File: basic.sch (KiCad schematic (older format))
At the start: 9 parts, among them J5 Conn_02x02_Top_Bottom, X1 dummy, X2 dummy

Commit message: Power Sch. Updated.
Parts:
- gave numbers to parts that had none: 4
- renumbered FID2 to FID3, J5 to J1
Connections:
- net GND renamed VIN_GND
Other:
- note removed: "TODO\n- breakout modem signals\n- TI DCDC might need to be set to 3.4V, \ncheck datasheets of all the stuff\n- MCP73223 UVLO is too low?\n- OPAMP for sense"
- moved on the sheet: J1
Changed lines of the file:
@@
 $EndComp
 Wire Wire Line
-	2850 3500 2650 3500
-$Comp
-L Mechanical:Fiducial FID2
+	3200 3550 3000 3550
+$Comp
+L Mechanical:Fiducial FID3
 U 1 1 5E789C24
 P 7700 5900
-F 0 "FID2" H 7785 5946 50  0000 L CNN
+F 0 "FID3" H 7785 5946 50  0000 L CNN
 F 1 "Fiducial" H 7785 5855 50  0000 L CNN
 F 2 "Aesthetics:FIDUCIAL-1X2" H 7700 5900 50  0001 C CNN
@@
 	1    0    0    -1
 $EndComp
-Text GLabel 2850 3500 2    50   Input ~ 0
+Text GLabel 3200 3550 2    50   Input ~ 0
 VIN_12V
 $Comp
-L Connector_Generic:Conn_02x02_Top_Bottom J5
+L Connector_Generic:Conn_02x02_Top_Bottom J1
 U 1 1 5E789BF0
-P 2350 3500
-F 0 "J5" H 2400 3250 50  0000 C CNN
-F 1 "Conn_02x02_Top_Bottom" H 2400 3700 50  0000 C CNN
-F 2 "Connector_Molex:Molex_Micro-Fit_3.0_43045-0400_2x02_P3.00mm_Horizontal" H 2350 3500 50  0001 C CNN
-F 3 "~" H 2350 3500 50  0001 C CNN
-	1    2350 3500
-	1    0    0    -1
-$EndComp
-Text Notes 950  6550 0    64   ~ 0
-TODO\n- breakout modem signals\n- TI  DCDC might need to be set to 3.4V, \ncheck datasheets of all the stuff\n- MCP73223 UVLO is too low?\n- OPAMP for sense
+P 2700 3550
+F 0 "J1" H 2750 3300 50  0000 C CNN
+F 1 "Conn_02x02_Top_Bottom" H 2750 3750 50  0000 C CNN
+F 2 "Connector_Molex:Molex_Micro-Fit_3.0_43045-0400_2x02_P3.00mm_Horizontal" H 2700 3550 50  0001 C CNN
+F 3 "~" H 2700 3550 50  0001 C CNN
+	1    2700 3550
+	1    0    0    -1
+$EndComp
 $Sheet
 S 4000 2400 1000 1000
@@
 F0 "power" 50
 F1 "power.sch" 50
+F2 "CHARGE_STAT" O R 5000 3100 50
+F3 "CHARGER_EN" I R 5000 3200 50
 $EndSheet
 $Comp
@@
 Wire Wire Line
 	5500 4400 5000 4400
-Text GLabel 2850 3600 2    50   Input ~ 0
+Text GLabel 3200 3650 2    50   Input ~ 0
 CANH
-Text GLabel 1900 3600 0    50   Input ~ 0
+Text GLabel 2250 3650 0    50   Input ~ 0
 CANL
 Wire Wire Line
-	2850 3600 2650 3600
+	3200 3650 3000 3650
 $Sheet
 S 5500 3000 1500 1500
@@
 F2 "TWIO_SCK" B R 7000 3100 50
 F3 "TWIO_SDA" B R 7000 3200 50
-F4 "CHARGE_STAT" I L 5500 3100 50
-F5 "CAN0IRQ" I L 5500 4400 50
-F6 "MISO" I L 5500 4000 50
-F7 "MOSI" O L 5500 4100 50
-F8 "SCLK" O L 5500 4200 50
-F9 "CSO" O L 5500 4300 50
-F10 "MODEM_TX" I R 7000 4300 50
-F11 "MODEM_RX" O R 7000 4400 50
-F12 "MODEM_RELAIS" O R 7000 4100 50
-F13 "MODEM_DTR" O R 7000 3900 50
-F14 "MODEM_WDISABLE" O R 7000 4200 50
-F15 "MODEM_RESET" O R 7000 4000 50
-F16 "IMU_INT1" I R 7000 3300 50
-$EndSheet
-$Comp
-L Mechanical:Fiducial FID?
+F4 "CAN0IRQ" I L 5500 4400 50
+F5 "MISO" I L 5500 4000 50
+F6 "MOSI" O L 5500 4100 50
+F7 "SCLK" O L 5500 4200 50
+F8 "CSO" O L 5500 4300 50
+F9 "MODEM_TX" I R 7000 4300 50
+F10 "MODEM_RX" O R 7000 4400 50
+F11 "MODEM_RELAIS" O R 7000 4100 50
+F12 "MODEM_DTR" O R 7000 3900 50
+F13 "MODEM_WDISABLE" O R 7000 4200 50
+F14 "MODEM_RESET" O R 7000 4000 50
+F15 "IMU_INT1" I R 7000 3300 50
+F16 "CHARGE_STAT" I L 5500 3100 50
+F17 "CHARGER_EN" O L 5500 3200 50
+$EndSheet
+$Comp
+L Mechanical:Fiducial FID5
 U 1 1 605974C2
 P 8200 5900
-F 0 "FID?" H 8285 5946 50  0000 L CNN
+F 0 "FID5" H 8285 5946 50  0000 L CNN
 F 1 "Fiducial" H 8285 5855 50  0000 L CNN
 F 2 "Aesthetics:FIDUCIAL-1X2" H 8200 5900 50  0001 C CNN
@@
 $EndComp
 $Comp
-L Mechanical:Fiducial FID?
+L Mechanical:Fiducial FID2
 U 1 1 60597847
 P 7150 6150
-F 0 "FID?" H 7235 6196 50  0000 L CNN
+F 0 "FID2" H 7235 6196 50  0000 L CNN
 F 1 "Fiducial" H 7235 6105 50  0000 L CNN
 F 2 "Aesthetics:FIDUCIAL-1X2" H 7150 6150 50  0001 C CNN
@@
 $EndComp
 $Comp
-L Mechanical:Fiducial FID?
+L Mechanical:Fiducial FID4
 U 1 1 60597BC6
 P 7700 6150
-F 0 "FID?" H 7785 6196 50  0000 L CNN
+F 0 "FID4" H 7785 6196 50  0000 L CNN
 F 1 "Fiducial" H 7785 6105 50  0000 L CNN
 F 2 "Aesthetics:FIDUCIAL-1X2" H 7700 6150 50  0001 C CNN
@@
 $EndComp
 $Comp
-L Mechanical:Fiducial FID?
+L Mechanical:Fiducial FID6
 U 1 1 60597F21
 P 8200 6150
-F 0 "FID?" H 8285 6196 50  0000 L CNN
+F 0 "FID6" H 8285 6196 50  0000 L CNN
 F 1 "Fiducial" H 8285 6105 50  0000 L CNN
 F 2 "Aesthetics:FIDUCIAL-1X2" H 8200 6150 50  0001 C CNN
@@
 	1    0    0    -1
 $EndComp
-$Comp
-L power:GND #PWR?
-U 1 1 6059A4E7
-P 2150 3500
-AR Path="/603BB897/6059A4E7" Ref="#PWR?"  Part="1"
-AR Path="/6059A4E7" Ref="#PWR?"  Part="1"
-F 0 "#PWR?" H 2150 3250 50  0001 C CNN
-F 1 "GND" H 2155 3327 50  0000 C CNN
-F 2 "" H 2150 3500 50  0001 C CNN
-F 3 "" H 2150 3500 50  0001 C CNN
-	1    2150 3500
-	0    1    1    0
-$EndComp
-Wire Wire Line
-	1900 3600 2150 3600
+Wire Wire Line
+	2250 3650 2500 3650
 $Sheet
 S 7500 3600 1000 1000
@@
 Wire Wire Line
 	7000 4400 7500 4400
+Text GLabel 2250 3550 0    50   Input ~ 0
+VIN_GND
+Wire Wire Line
+	2500 3550 2250 3550
+Wire Wire Line
+	5000 3100 5500 3100
+Wire Wire Line
+	5000 3200 5500 3200
 $EndSCHEMATC

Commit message: Updated power mux with LM73100.
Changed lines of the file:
@@
 F2 "CHARGE_STAT" O R 5000 3100 50
 F3 "CHARGER_EN" I R 5000 3200 50
+F4 "IN1_PG" O R 5000 3000 50
+F5 "IN2_PG" O R 5000 2900 50
 $EndSheet
 $Comp

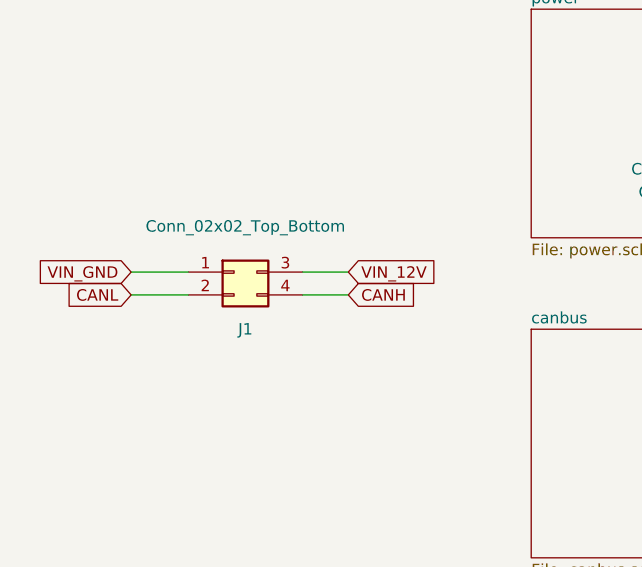
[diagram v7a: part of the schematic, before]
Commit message: Power section routing completed.
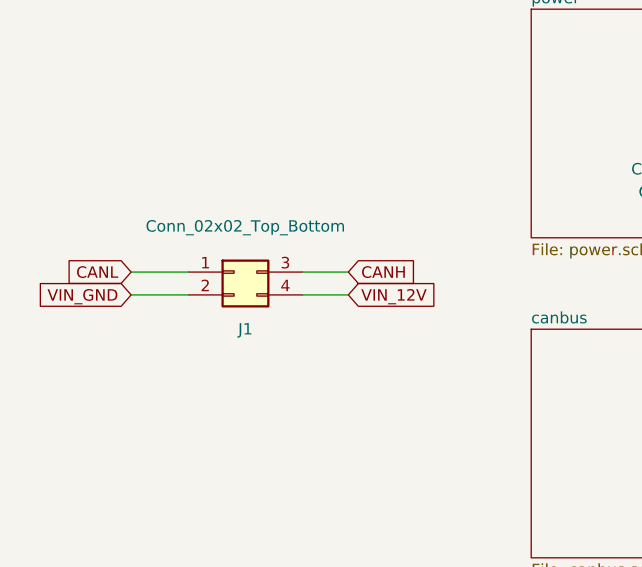
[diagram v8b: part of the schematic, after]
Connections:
- net CANH: now also J1.3 (Pin_3); no longer J1.4 (Pin_4)
- net CANL: now also J1.1 (Pin_1); no longer J1.2 (Pin_2)
- net VIN_12V: now also J1.4 (Pin_4); no longer J1.3 (Pin_3)
- net VIN_GND: now also J1.2 (Pin_2); no longer J1.1 (Pin_1)
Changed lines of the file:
@@
 Wire Wire Line
 	5000 3200 5500 3200
+Text GLabel 3200 3650 2    50   Input ~ 0
+VIN_12V
+Wire Wire Line
+	3200 3650 3000 3650
+Wire Wire Line
+	2250 3550 2500 3550
+Text GLabel 2250 3550 0    50   Input ~ 0
+CANL
 Text GLabel 3200 3550 2    50   Input ~ 0
-VIN_12V
+CANH
 Wire Wire Line
 	3200 3550 3000 3550
 Wire Wire Line
-	2250 3650 2500 3650
+	2500 3650 2250 3650
 Text GLabel 2250 3650 0    50   Input ~ 0
-CANL
-Text GLabel 3200 3650 2    50   Input ~ 0
-CANH
-Wire Wire Line
-	3200 3650 3000 3650
-Wire Wire Line
-	2500 3550 2250 3550
-Text GLabel 2250 3550 0    50   Input ~ 0
 VIN_GND
 $EndSCHEMATC
